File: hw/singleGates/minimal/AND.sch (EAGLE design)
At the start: 8 parts, among them Q1 BC817, Q2 BC817, Q3 BC817

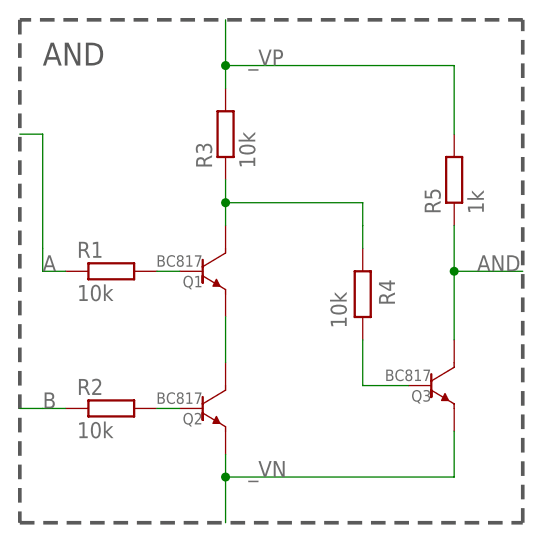
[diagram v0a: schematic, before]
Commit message: Add led output and prepare first alu slice
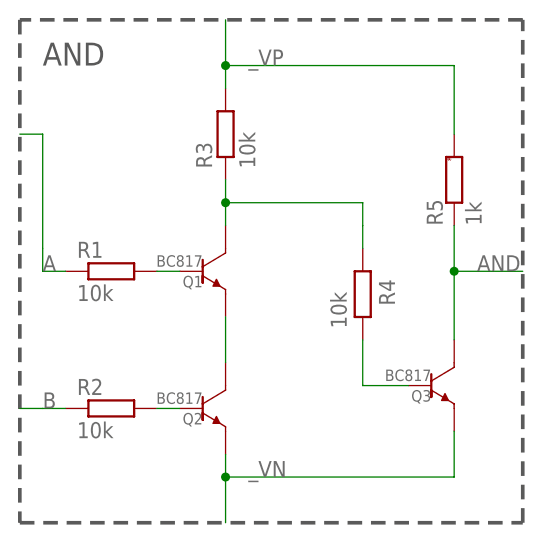
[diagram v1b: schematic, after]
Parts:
- R5: device p.peter-gator:R-EU_R0603 -> p.peter-rcl:R-EU-MARKEDR0603
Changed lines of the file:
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@@
 <part name="R3" library="p.peter-gator" deviceset="R-EU_" device="R0603" value="10k"/>
 <part name="R4" library="p.peter-gator" deviceset="R-EU_" device="R0603" value="10k"/>
-<part name="R5" library="p.peter-gator" deviceset="R-EU_" device="R0603" value="1k"/>
+<part name="R5" library="p.peter-rcl" deviceset="R-EU-MARKED" device="R0603" value="1k"/>
 <part name="Q1" library="p.peter-gator" deviceset="TRANSISTOR-NPN-GENERIC" device="-SOT23-BEC" technology="DEFAULT" value="BC817"/>
 <part name="Q2" library="p.peter-gator" deviceset="TRANSISTOR-NPN-GENERIC" device="-SOT23-BEC" technology="DEFAULT" value="BC817"/>
